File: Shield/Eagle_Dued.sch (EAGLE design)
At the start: 75 parts, among them IC1 7805TV, IC2 LM340MP-05

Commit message: Additional corrections and goodness for the shields.
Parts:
- added JP3: (no value), jumper:JP1E
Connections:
- new net N$1: JP3.1, POWER.5
- net +5V: now also JP3.2; no longer POWER.5
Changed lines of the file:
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@@
 <part name="GND25" library="supply1" deviceset="GND" device=""/>
 <part name="JP1" library="SparkFun-Connectors" deviceset="M04" device="POLAR"/>
+<part name="JP3" library="jumper" deviceset="JP1E" device=""/>
 </parts>
 <sheets>
@@
 </instance>
 <instance part="GND5" gate="1" x="429.26" y="170.18"/>
-<instance part="P+4" gate="1" x="429.26" y="200.66" smashed="yes">
-<attribute name="VALUE" x="431.165" y="203.2" size="1.778" layer="96" rot="R180"/>
+<instance part="P+4" gate="1" x="411.48" y="182.88" smashed="yes" rot="R90">
+<attribute name="VALUE" x="408.94" y="184.785" size="1.778" layer="96" rot="R270"/>
 </instance>
 <instance part="POWER" gate="A" x="452.12" y="182.88"/>
@@
 <instance part="GND25" gate="1" x="510.54" y="88.9" rot="R90"/>
 <instance part="JP1" gate="G$1" x="449.58" y="137.16"/>
+<instance part="JP3" gate="A" x="424.18" y="180.34" rot="R180"/>
 </instances>
 <busses>
@@
 <nets>
 <net name="+5V" class="0">
-<segment>
-<wire x1="449.58" y1="182.88" x2="429.26" y2="182.88" width="0.1524" layer="91"/>
-<wire x1="429.26" y1="182.88" x2="429.26" y2="198.12" width="0.1524" layer="91"/>
-<pinref part="P+4" gate="1" pin="+5V"/>
-<pinref part="POWER" gate="A" pin="5"/>
-</segment>
 <segment>
 <wire x1="360.68" y1="157.48" x2="353.06" y2="157.48" width="0.1524" layer="91"/>
@@
 <wire x1="543.56" y1="149.86" x2="525.78" y2="149.86" width="0.1524" layer="91"/>
 <label x="525.78" y="149.86" size="1.778" layer="95"/>
+</segment>
+<segment>
+<pinref part="JP3" gate="A" pin="2"/>
+<pinref part="P+4" gate="1" pin="+5V"/>
+<wire x1="421.64" y1="182.88" x2="414.02" y2="182.88" width="0.1524" layer="91"/>
 </segment>
 </net>
@@
 </segment>
 </net>
+<net name="N$1" class="0">
+<segment>
+<wire x1="449.58" y1="182.88" x2="424.18" y2="182.88" width="0.1524" layer="91"/>
+<pinref part="POWER" gate="A" pin="5"/>
+<pinref part="JP3" gate="A" pin="1"/>
+</segment>
+</net>

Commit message: updated dued board to fit a different case.
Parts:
- removed JP2, JP3: (no value), jumper:JP1E
- added SJ5, SJ6: SOLDERJUMPERNO, SparkFun-Passives:SOLDERJUMPERNO
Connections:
- new net +5V\: U$3.28
- net +12V: now also SJ5.1, U$3.5, U$3.6; no longer JP2.1, U$3.30, U$3.31
- net +5V: now also SJ6.2, U$3.25, U$3.27; no longer JP3.2, U$3.20, U$3.22, U$3.8
- net AIN1: now also U$3.20; no longer U$3.21
- net AIN2: now also U$3.21; no longer U$3.23
- net AIN3: now also U$3.22; no longer U$3.25
- net AIN4: now also U$3.23; no longer U$3.27
- net GND: now also U$3.30, U$3.31, U$3.8; no longer U$3.28, U$3.5, U$3.6
- net N$1: now also SJ6.1; no longer JP3.1
- net VIN: now also SJ5.2; no longer JP2.2
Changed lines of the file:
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@@
 <part name="+3V1" library="supply1" deviceset="+3V3" device=""/>
 <part name="P+3" library="supply1" deviceset="+5V" device=""/>
-<part name="JP2" library="jumper" deviceset="JP1E" device=""/>
 <part name="D2" library="SparkFun-LED" deviceset="LED-GREEN" device="0603" value="GREEN"/>
 <part name="D3" library="SparkFun-LED" deviceset="LED-GREEN" device="0603" value="GREEN"/>
@@
 <part name="GND25" library="supply1" deviceset="GND" device=""/>
 <part name="JP1" library="SparkFun-Connectors" deviceset="M04" device="POLAR"/>
-<part name="JP3" library="jumper" deviceset="JP1E" device=""/>
+<part name="SJ5" library="SparkFun-Passives" deviceset="SOLDERJUMPER" device="NO"/>
+<part name="SJ6" library="SparkFun-Passives" deviceset="SOLDERJUMPER" device="NO"/>
 </parts>
 <sheets>
@@
 <instance part="+3V1" gate="G$1" x="558.8" y="-17.78"/>
 <instance part="P+3" gate="1" x="314.96" y="-5.08"/>
-<instance part="JP2" gate="A" x="322.58" y="-12.7" rot="R90"/>
 <instance part="D2" gate="G$1" x="500.38" y="-15.24" rot="R90"/>
 <instance part="D3" gate="G$1" x="533.4" y="-15.24" rot="R270"/>
@@
 <instance part="GND25" gate="1" x="510.54" y="88.9" rot="R90"/>
 <instance part="JP1" gate="G$1" x="449.58" y="137.16"/>
-<instance part="JP3" gate="A" x="424.18" y="180.34" rot="R180"/>
+<instance part="SJ5" gate="1" x="325.12" y="-10.16" smashed="yes" rot="R90">
+<attribute name="NAME" x="322.58" y="-12.7" size="1.778" layer="95" rot="R90"/>
+</instance>
+<instance part="SJ6" gate="1" x="421.64" y="182.88" smashed="yes" rot="R180">
+<attribute name="NAME" x="424.18" y="180.34" size="1.778" layer="95" rot="R180"/>
+</instance>
 </instances>
 <busses>
@@
 </segment>
 <segment>
-<pinref part="U$3" gate="G$1" pin="20"/>
-<wire x1="551.18" y1="165.1" x2="571.5" y2="165.1" width="0.1524" layer="91"/>
-<label x="566.42" y="165.1" size="1.778" layer="95"/>
-</segment>
-<segment>
-<pinref part="U$3" gate="G$1" pin="22"/>
-<wire x1="551.18" y1="160.02" x2="571.5" y2="160.02" width="0.1524" layer="91"/>
-<label x="566.42" y="160.02" size="1.778" layer="95"/>
-</segment>
-<segment>
 <pinref part="U$3" gate="G$1" pin="24"/>
 <wire x1="551.18" y1="154.94" x2="571.5" y2="154.94" width="0.1524" layer="91"/>
@@
 </segment>
 <segment>
-<pinref part="U$3" gate="G$1" pin="8"/>
-<wire x1="543.56" y1="149.86" x2="525.78" y2="149.86" width="0.1524" layer="91"/>
-<label x="525.78" y="149.86" size="1.778" layer="95"/>
-</segment>
-<segment>
-<pinref part="JP3" gate="A" pin="2"/>
+<pinref part="SJ6" gate="1" pin="2"/>
 <pinref part="P+4" gate="1" pin="+5V"/>
-<wire x1="421.64" y1="182.88" x2="414.02" y2="182.88" width="0.1524" layer="91"/>
+<wire x1="416.56" y1="182.88" x2="414.02" y2="182.88" width="0.1524" layer="91"/>
+</segment>
+<segment>
+<pinref part="U$3" gate="G$1" pin="25"/>
+<wire x1="551.18" y1="152.4" x2="571.5" y2="152.4" width="0.1524" layer="91"/>
+<label x="566.42" y="152.4" size="1.778" layer="95"/>
+</segment>
+<segment>
+<wire x1="551.18" y1="147.32" x2="571.5" y2="147.32" width="0.1524" layer="91"/>
+<label x="566.42" y="147.32" size="1.778" layer="95"/>
+<pinref part="U$3" gate="G$1" pin="27"/>
 </segment>
 </net>
@@
 </segment>
 <segment>
-<pinref part="U$3" gate="G$1" pin="6"/>
-<wire x1="543.56" y1="154.94" x2="525.78" y2="154.94" width="0.1524" layer="91"/>
-<label x="525.78" y="154.94" size="1.778" layer="95"/>
-</segment>
-<segment>
-<pinref part="U$3" gate="G$1" pin="5"/>
-<wire x1="543.56" y1="157.48" x2="525.78" y2="157.48" width="0.1524" layer="91"/>
-<label x="525.78" y="157.48" size="1.778" layer="95"/>
-</segment>
-<segment>
 <pinref part="U$3" gate="G$1" pin="19"/>
 <wire x1="551.18" y1="167.64" x2="571.5" y2="167.64" width="0.1524" layer="91"/>
@@
 </segment>
 <segment>
-<wire x1="551.18" y1="144.78" x2="571.5" y2="144.78" width="0.1524" layer="91"/>
-<label x="563.88" y="144.78" size="1.778" layer="95"/>
-<pinref part="U$3" gate="G$1" pin="28"/>
-</segment>
-<segment>
 <wire x1="551.18" y1="142.24" x2="571.5" y2="142.24" width="0.1524" layer="91"/>
 <label x="563.88" y="142.24" size="1.778" layer="95"/>
 <pinref part="U$3" gate="G$1" pin="29"/>
 </segment>
+<segment>
+<pinref part="U$3" gate="G$1" pin="8"/>
+<wire x1="543.56" y1="149.86" x2="525.78" y2="149.86" width="0.1524" layer="91"/>
+<label x="525.78" y="149.86" size="1.778" layer="95"/>
+</segment>
+<segment>
+<wire x1="551.18" y1="139.7" x2="571.5" y2="139.7" width="0.1524" layer="91"/>
+<label x="563.88" y="139.7" size="1.778" layer="95"/>
+<pinref part="U$3" gate="G$1" pin="30"/>
+</segment>
+<segment>
+<pinref part="U$3" gate="G$1" pin="31"/>
+<wire x1="551.18" y1="137.16" x2="571.5" y2="137.16" width="0.1524" layer="91"/>
+<label x="563.88" y="137.16" size="1.778" layer="95"/>
+</segment>
 </net>
 <net name="VIN" class="0">
@@
 </segment>
 <segment>
-<pinref part="JP2" gate="A" pin="2"/>
-<wire x1="325.12" y1="-10.16" x2="325.12" y2="2.54" width="0.1524" layer="91"/>
 <wire x1="325.12" y1="2.54" x2="335.28" y2="2.54" width="0.1524" layer="91"/>
 <label x="330.2" y="2.54" size="1.778" layer="95"/>
+<pinref part="SJ5" gate="1" pin="2"/>
+<wire x1="325.12" y1="-5.08" x2="325.12" y2="2.54" width="0.1524" layer="91"/>
 </segment>
 </net>
@@
 <segment>
 <wire x1="299.72" y1="-22.86" x2="325.12" y2="-22.86" width="0.1524" layer="91"/>
-<wire x1="325.12" y1="-22.86" x2="325.12" y2="-12.7" width="0.1524" layer="91"/>
-<pinref part="JP2" gate="A" pin="1"/>
 <label x="299.72" y="-22.86" size="1.778" layer="95"/>
+<pinref part="SJ5" gate="1" pin="1"/>
+<wire x1="325.12" y1="-22.86" x2="325.12" y2="-15.24" width="0.1524" layer="91"/>
 </segment>
 <segment>
@@
 </segment>
 <segment>
-<pinref part="U$3" gate="G$1" pin="31"/>
-<wire x1="551.18" y1="137.16" x2="571.5" y2="137.16" width="0.1524" layer="91"/>
-<label x="563.88" y="137.16" size="1.778" layer="95"/>
-</segment>
-<segment>
-<wire x1="551.18" y1="139.7" x2="571.5" y2="139.7" width="0.1524" layer="91"/>
-<label x="563.88" y="139.7" size="1.778" layer="95"/>
-<pinref part="U$3" gate="G$1" pin="30"/>
-</segment>
-<segment>
 <pinref part="U$3" gate="G$1" pin="3"/>
 <wire x1="543.56" y1="162.56" x2="525.78" y2="162.56" width="0.1524" layer="91"/>
@@
 <label x="525.78" y="160.02" size="1.778" layer="95"/>
 </segment>
+<segment>
+<pinref part="U$3" gate="G$1" pin="5"/>
+<wire x1="543.56" y1="157.48" x2="525.78" y2="157.48" width="0.1524" layer="91"/>
+<label x="525.78" y="157.48" size="1.778" layer="95"/>
+</segment>
+<segment>
+<pinref part="U$3" gate="G$1" pin="6"/>
+<wire x1="543.56" y1="154.94" x2="525.78" y2="154.94" width="0.1524" layer="91"/>
+<label x="525.78" y="154.94" size="1.778" layer="95"/>
+</segment>
 </net>
 <net name="AIN3" class="0">
-<segment>
-<pinref part="U$3" gate="G$1" pin="25"/>
-<wire x1="551.18" y1="152.4" x2="571.5" y2="152.4" width="0.1524" layer="91"/>
-<label x="566.42" y="152.4" size="1.778" layer="95"/>
-</segment>
 <segment>
 <pinref part="JP1" gate="G$1" pin="3"/>
@@
 <label x="467.36" y="139.7" size="1.778" layer="95"/>
 </segment>
+<segment>
+<pinref part="U$3" gate="G$1" pin="22"/>
+<wire x1="551.18" y1="160.02" x2="571.5" y2="160.02" width="0.1524" layer="91"/>
+<label x="566.42" y="160.02" size="1.778" layer="95"/>
+</segment>
 </net>
 <net name="AIN2" class="0">
-<segment>
-<pinref part="U$3" gate="G$1" pin="23"/>
-<wire x1="551.18" y1="157.48" x2="571.5" y2="157.48" width="0.1524" layer="91"/>
-<label x="566.42" y="157.48" size="1.778" layer="95"/>
-</segment>
 <segment>
 <pinref part="JP1" gate="G$1" pin="2"/>
@@
 <label x="467.36" y="137.16" size="1.778" layer="95"/>
 </segment>
-</net>
-<net name="AIN1" class="0">
 <segment>
 <pinref part="U$3" gate="G$1" pin="21"/>
@@
 <label x="566.42" y="162.56" size="1.778" layer="95"/>
 </segment>
+</net>
+<net name="AIN1" class="0">
 <segment>
 <pinref part="JP1" gate="G$1" pin="1"/>
 <wire x1="454.66" y1="134.62" x2="472.44" y2="134.62" width="0.1524" layer="91"/>
 <label x="467.36" y="134.62" size="1.778" layer="95"/>
+</segment>
+<segment>
+<pinref part="U$3" gate="G$1" pin="20"/>
+<wire x1="551.18" y1="165.1" x2="571.5" y2="165.1" width="0.1524" layer="91"/>
+<label x="566.42" y="165.1" size="1.778" layer="95"/>
 </segment>
 </net>
@@
 <net name="AIN4" class="0">
 <segment>
-<wire x1="551.18" y1="147.32" x2="571.5" y2="147.32" width="0.1524" layer="91"/>
-<label x="563.88" y="147.32" size="1.778" layer="95"/>
-<pinref part="U$3" gate="G$1" pin="27"/>
-</segment>
-<segment>
 <pinref part="JP1" gate="G$1" pin="4"/>
 <wire x1="454.66" y1="142.24" x2="472.44" y2="142.24" width="0.1524" layer="91"/>
 <label x="467.36" y="142.24" size="1.778" layer="95"/>
 </segment>
+<segment>
+<pinref part="U$3" gate="G$1" pin="23"/>
+<wire x1="551.18" y1="157.48" x2="571.5" y2="157.48" width="0.1524" layer="91"/>
+<label x="566.42" y="157.48" size="1.778" layer="95"/>
+</segment>
 </net>
 <net name="N$1" class="0">
 <segment>
-<wire x1="449.58" y1="182.88" x2="424.18" y2="182.88" width="0.1524" layer="91"/>
+<wire x1="449.58" y1="182.88" x2="426.72" y2="182.88" width="0.1524" layer="91"/>
 <pinref part="POWER" gate="A" pin="5"/>
-<pinref part="JP3" gate="A" pin="1"/>
-</segment>
-</net>
+<pinref part="SJ6" gate="1" pin="1"/>
+</segment>
+</net>
+<net name="+5V\" class="0">
+<segment>
+<wire x1="551.18" y1="144.78" x2="571.5" y2="144.78" width="0.1524" layer="91"/>
+<label x="566.42" y="144.78" size="1.778" layer="95"/>
+<pinref part="U$3" gate="G$1" pin="28"/>
+</segment>
+</net>

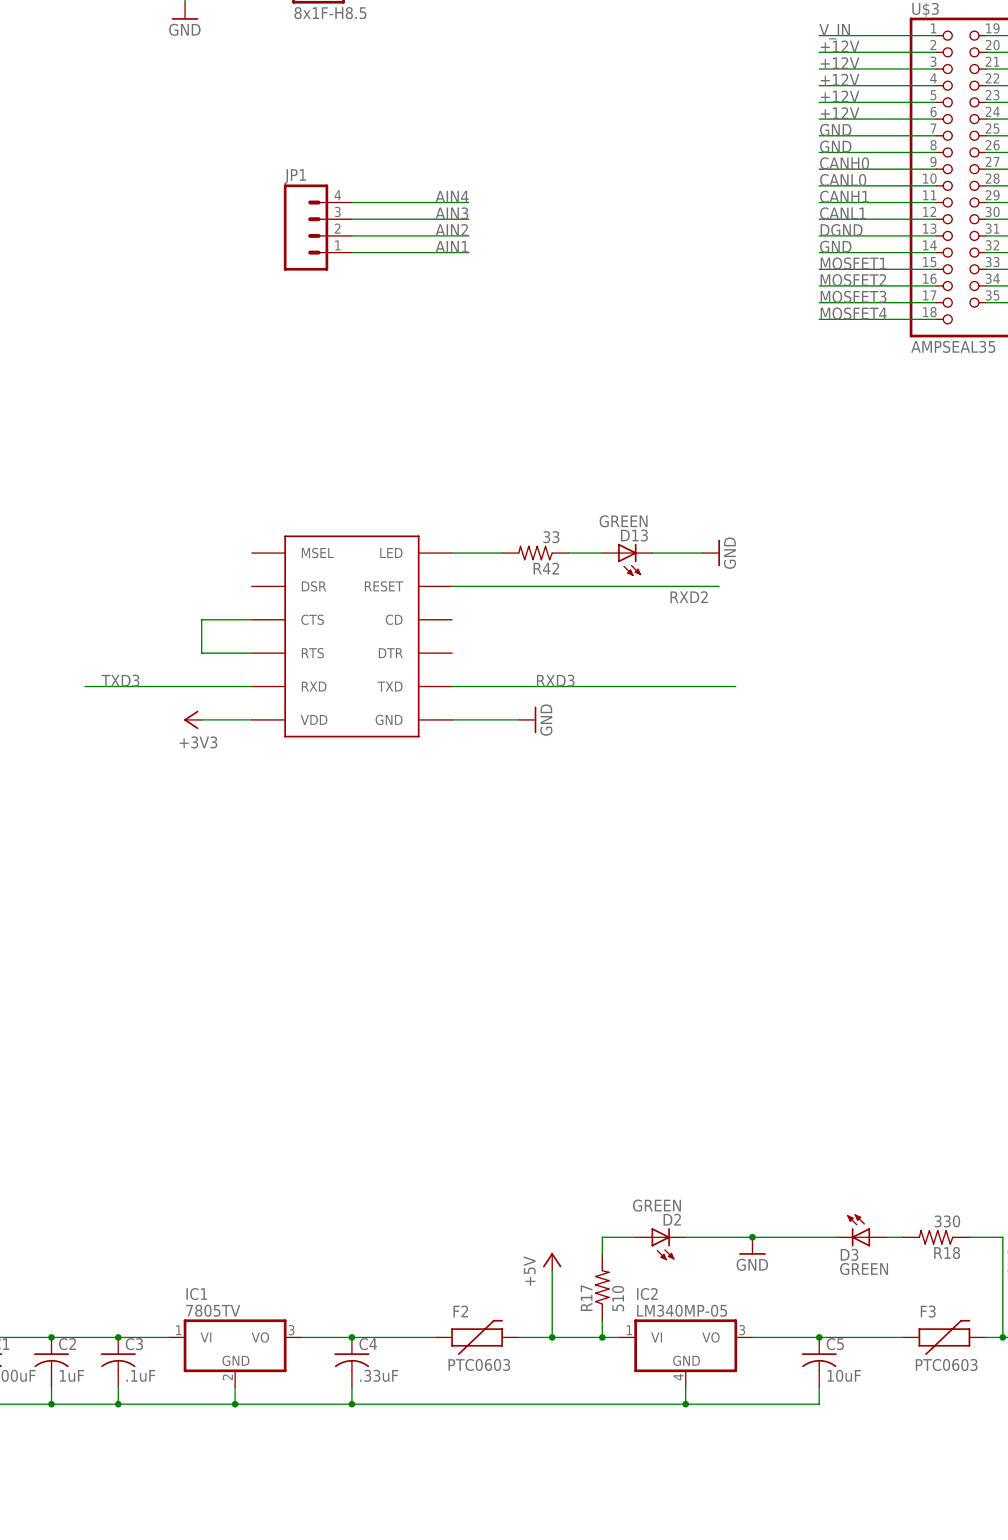
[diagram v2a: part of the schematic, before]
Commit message: Updated canbus board to fix a layout issue, updated DueD to use DC/DC converter
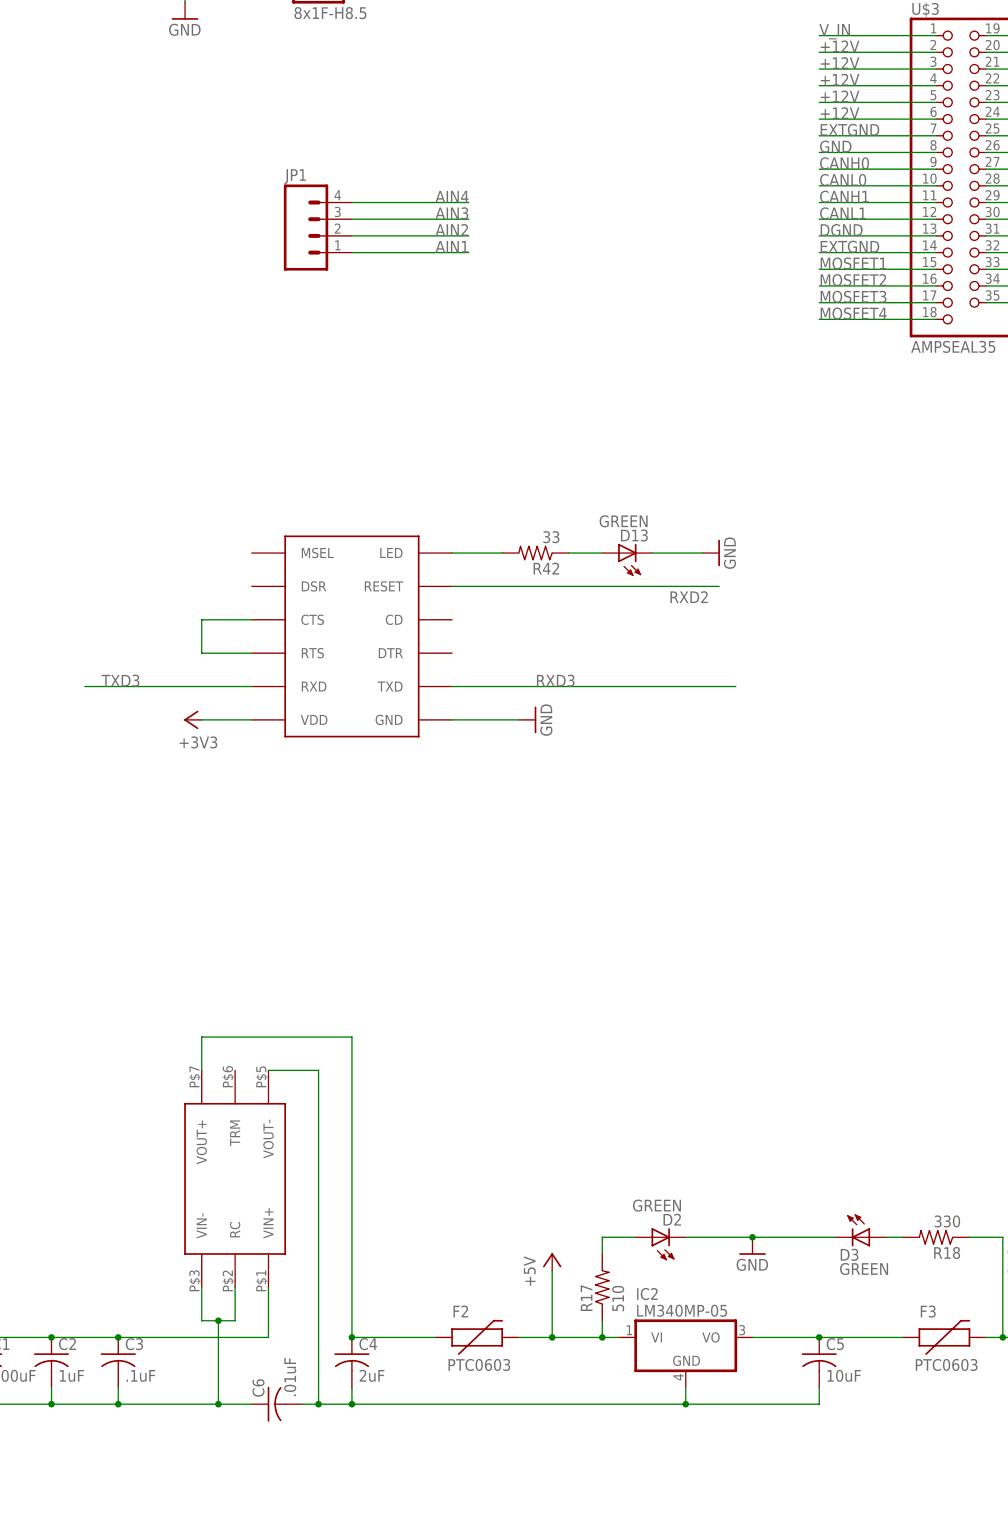
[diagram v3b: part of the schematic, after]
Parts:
- removed IC1: 7805TV, linear:7805TV
- added C6: .01uF, rcl:C-USC1206
- added U$1: CC3-E, dc-dc-converter:CC3-E
- C4: value .33uF -> 2uF
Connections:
- new net EXTGND: C1.-, C2.2, C3.2, C6.1, D1.A, D4.A, D5.A, D6.A, OK1A.C, OK1A.EMIT, OK1B.C, OK1B.EMIT, OK2A.C, OK2A.EMIT, OK2B.C, OK2B.EMIT, R25.2, R26.2, R27.2, R28.2, T1.S, T2.S, T3.S, T4.S, U$1.RC, U$1.VIN-, U$3.14, U$3.7, U$8.A, U$9.1
- net +12V: now also U$1.VIN+; no longer IC1.VI
- net GND: now also C6.2, U$1.VOUT-; no longer C1.-, C2.2, C3.2, D1.A, D4.A, D5.A, D6.A, IC1.GND, OK1A.C, OK1A.EMIT, OK1B.C, OK1B.EMIT, OK2A.C, OK2A.EMIT, OK2B.C, OK2B.EMIT, R25.2, R26.2, R27.2, R28.2, T1.S, T2.S, T3.S, T4.S, U$3.14, U$3.7, U$8.A, U$9.1
- net N$6: now also U$1.VOUT+; no longer IC1.VO

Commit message: Added optocouplers to mosfet outputs
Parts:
- added C7, C8: .1uF, rcl:C-USC1206
- added R1, R2, R3, R4: 560, rcl:R-US_R0603
- added U$10, U$7: SFH6731, ck_custom:SFH6731
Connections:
- new net 0V: C7.2, C8.2, OK1A.C, OK1B.C, OK2A.C, OK2B.C, U$10.GND, U$7.GND
- new net MDRIVE1: R25.1, T1.G, U$10.VO1
- new net MDRIVE2: R26.1, T2.G, U$10.VO2
- new net MDRIVE3: R27.1, T3.G, U$7.VO1
- new net MDRIVE4: R28.1, T4.G, U$7.VO2
- new net N$10: R2.2, U$10.A2
- new net N$11: R4.2, U$7.A2
- new net N$5: R3.2, U$7.A1
- new net N$7: R1.2, U$10.A1
- net +12V: now also C7.1, C8.1, U$10.VCC, U$7.VCC
- net DIGOUT1: now also R1.1; no longer R25.1, T1.G
- net DIGOUT2: now also R2.1; no longer R26.1, T2.G
- net DIGOUT3: now also R3.1; no longer R27.1, T3.G
- net DIGOUT4: now also R4.1; no longer R28.1, T4.G
- net EXTGND: now also L1.2; no longer OK1A.C, OK1A.EMIT, OK1B.C, OK1B.EMIT, OK2A.C, OK2A.EMIT, OK2B.C, OK2B.EMIT
- net GND: now also OK1A.EMIT, OK1B.EMIT, OK2A.EMIT, OK2B.EMIT, U$10.C1, U$10.C2, U$7.C1, U$7.C2; no longer L1.2
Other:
- moved on the sheet: D4, R26, T2
